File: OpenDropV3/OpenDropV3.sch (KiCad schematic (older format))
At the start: 257 parts, among them J1 USB_C_Receptacle, J2 Conn_02x05_Odd_Even, P1 CONN_01X01, P10 CONN_01X01, P11 CONN_01X01, P12 CONN_01X01, P13 ScrewPad1, P14 ScrewPad2, P15 ScrewPad3, P16 ScrewPad4, P2 ScrewPad4, P3 CONN_01X01, P4 CONN_PSEUDO_AC, P7 CONN_01X01, P8 CONN_01X01, P9 CONN_01X01, SW1 SW_PUSH, SW2 SW_PUSH, SW3 SW_PUSH, SW5 SPST, T1 TK560P60Y, U1 MAX1771ESA, U10 AQY210EH, U11 AQY210EH, U12 AQY210EH, U13 AQY210EH, U14 TLV1117-33, U15 MCP41010, U16 74xx14, U2 HV507, U3 PAM8301, U4 HV507, U5 SAMD21G18B-A changed from SAM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, U6 MCP6002, U7 HCPL0534, U8 HCPL0534, U9 HCPL0534, Y1 32.765

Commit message: Updatee Shem and footprints
Still needs to update the PCB design with new footprints
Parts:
- removed SW3: SW_PUSH, GaudiLabsFootPrints:SW_SPST_KMS221GLFS, symbol SW_PUSH
- added R14, R23: 5R1, GaudiLabsFootPrints:R_0805_HeatPad, symbol R
- added SW3: PTS810_SJK_250_SMTR_LFS, OpenBCI:PTS810, symbol PTS810_SJK_250_SMTR_LFS
- JS1: footprint GaudiLabsFootPrints:JoystickSMD_SKQUSeries -> Solutions:5P_Joystick_SKRHAAE010
- SW5: footprint GaudiLabsFootPrints:Switch_On-On -> Solutions:OS202011MA2QS1_DPDT
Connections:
- net GND: now also JS1.5 (Common), R14.2, R23.2, SW3.3, SW3.4; no longer JS1.6 (D_(down))
- net JOY: now also JS1.4 (B_(right)); no longer JS1.5 (Common)
- net RESET: now also SW3.1, SW3.2
- net SW3: now also JS1.2 (Center); no longer JS1.4 (B_(right))
- net at R20.1, R21.2: now also JS1.3 (C_(left)); no longer JS1.2 (Center)
- net at R19.1, R20.2: now also JS1.6 (D_(down)); no longer JS1.3 (C_(left))
- net at J1.A5 (CC1): now also R14.1, R23.1
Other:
- moved on the sheet: J1, R15, R16, R17, R7

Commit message: Adjusting PCB for more room around some components
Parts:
- C32: footprint Resistors_SMD:R_2512_HandSoldering -> Capacitors_SMD:C_1210_HandSoldering
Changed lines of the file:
@@
 F 0 "C32" H 13225 11450 50  0000 L CNN
 F 1 "100uF,50V" V 13050 11200 50  0000 L CNN
-F 2 "Resistors_SMD:R_2512_HandSoldering" H 13238 11200 30  0001 C CNN
+F 2 "Capacitors_SMD:C_1210_HandSoldering" H 13238 11200 30  0001 C CNN
 F 3 "" H 13200 11350 60  0000 C CNN
 	1    13200 11350

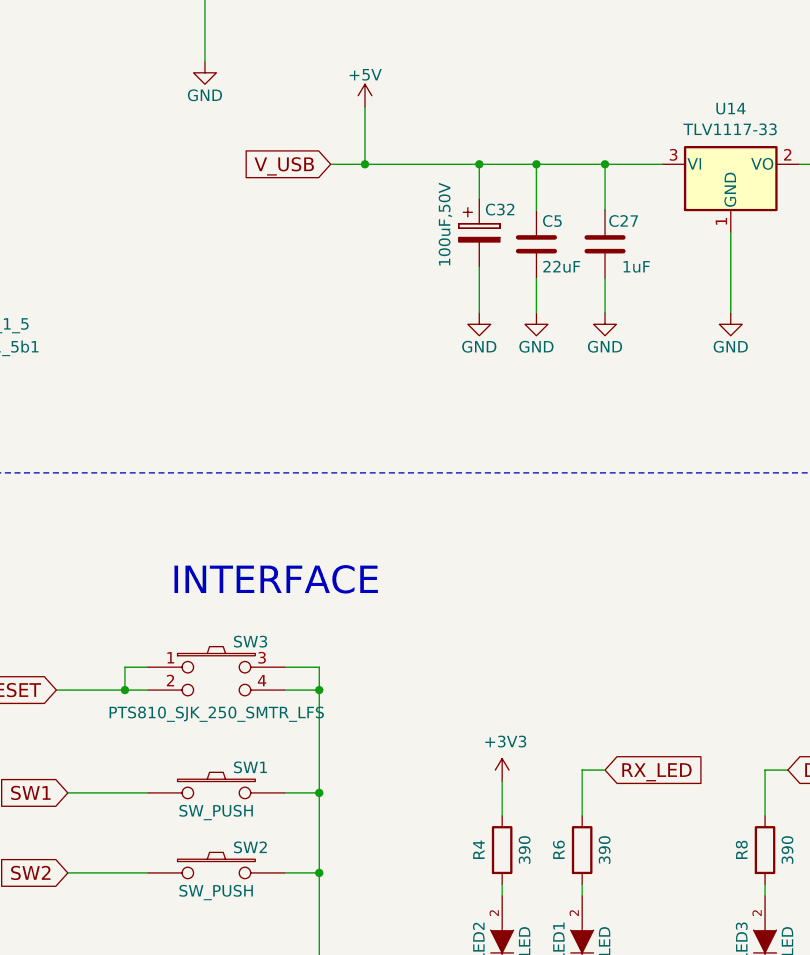
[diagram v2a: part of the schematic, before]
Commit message: Updated footprint associations
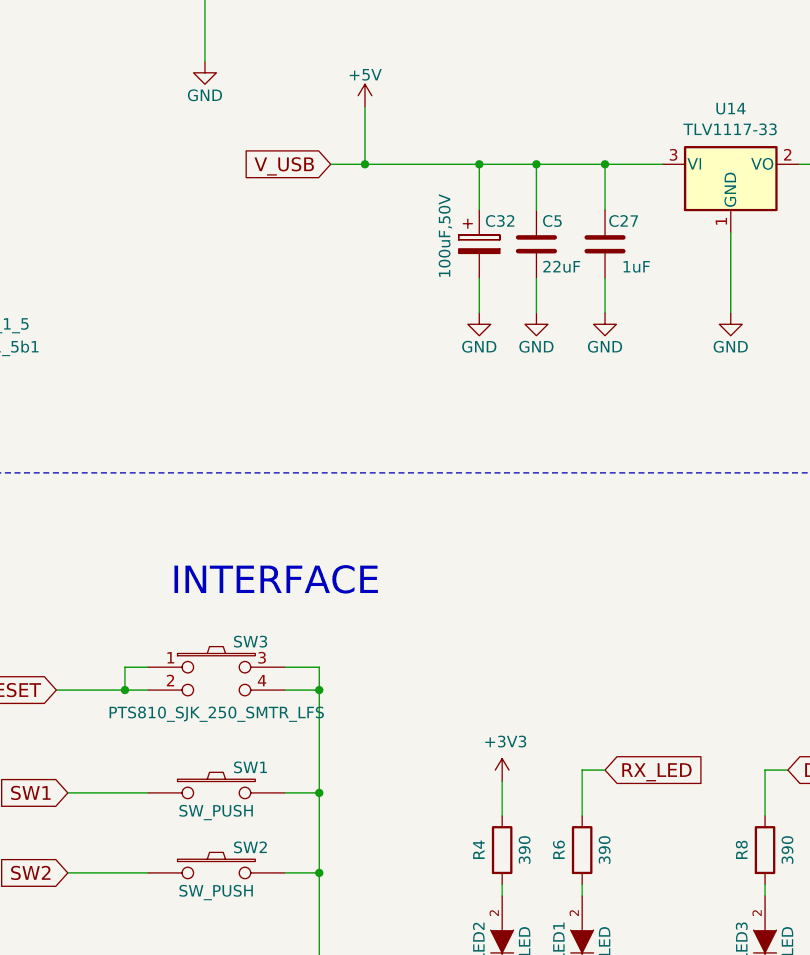
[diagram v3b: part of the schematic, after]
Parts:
- C32: footprint Capacitors_SMD:C_1210_HandSoldering -> Resistors_SMD:R_2512_HandSoldering
- C35, C6: footprint GaudiLabsFootPrints:C_1913 -> Capacitors_SMD:C_1206_HandSoldering
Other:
- moved on the sheet: C32
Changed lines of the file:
@@
 F 0 "C6" H 14575 2950 50  0000 L CNN
 F 1 "100nF, 250V" V 14400 2650 50  0000 L CNN
-F 2 "GaudiLabsFootPrints:C_1913" H 14588 2700 30  0001 C CNN
+F 2 "Capacitors_SMD:C_1206_HandSoldering" H 14588 2700 30  0001 C CNN
 F 3 "" H 14550 2850 60  0000 C CNN
 	1    14550 2850
@@
 L CP C32
 U 1 1 5A0D7DF2
-P 13200 11350
-F 0 "C32" H 13225 11450 50  0000 L CNN
-F 1 "100uF,50V" V 13050 11200 50  0000 L CNN
-F 2 "Capacitors_SMD:C_1210_HandSoldering" H 13238 11200 30  0001 C CNN
-F 3 "" H 13200 11350 60  0000 C CNN
-	1    13200 11350
+P 13200 11400
+F 0 "C32" H 13225 11500 50  0000 L CNN
+F 1 "100uF,50V" V 13050 11250 50  0000 L CNN
+F 2 "Resistors_SMD:R_2512_HandSoldering" H 13238 11250 30  0001 C CNN
+F 3 "" H 13200 11400 60  0000 C CNN
+	1    13200 11400
 	1    0    0    -1
 $EndComp
@@
 	8000 7550 8600 7550
 Wire Wire Line
-	12350 13800 12500 13800
+	12500 13800 12350 13800
 Wire Wire Line
 	12500 13250 12500 14800
@@
 Connection ~ 13200 11050
 Wire Wire Line
-	13200 11050 13200 11200
+	13200 11050 13200 11250
 Wire Wire Line
-	13200 11500 13200 11700
+	13200 11550 13200 11700
 Wire Wire Line
 	9800 2350 9800 2600
@@
 F 0 "C35" H 6525 3250 50  0000 L CNN
 F 1 "100nF, 250V" V 6350 2950 50  0000 L CNN
-F 2 "GaudiLabsFootPrints:C_1913" H 6538 3000 30  0001 C CNN
+F 2 "Capacitors_SMD:C_1206_HandSoldering" H 6538 3000 30  0001 C CNN
 F 3 "" H 6500 3150 60  0000 C CNN
 	1    6500 3150
